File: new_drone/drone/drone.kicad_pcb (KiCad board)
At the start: 2 copper layers, 100 x 100 mm, 61 parts, among them J1 Conn_01x06, J2 XT60-M, SW1 SW_Push_Open, SW2 SW_Push_Open, U1 MPU-6050, U2 ESP32-WROOM-32, U3 MCP8063, U4 BMP280, U5 MCP8063, U6 MCP8063, U7 MCP8063, U9 LM1117MP-3.3

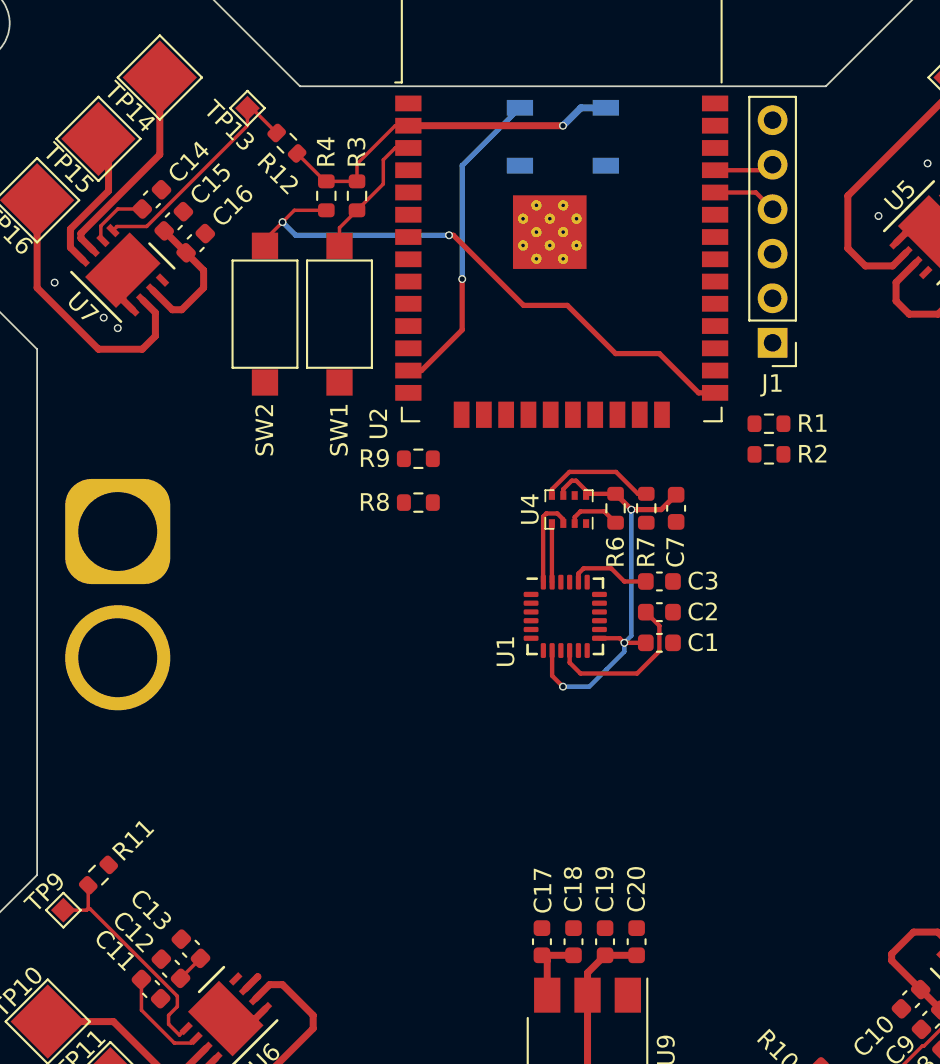
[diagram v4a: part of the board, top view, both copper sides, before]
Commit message: add openmv cam pin
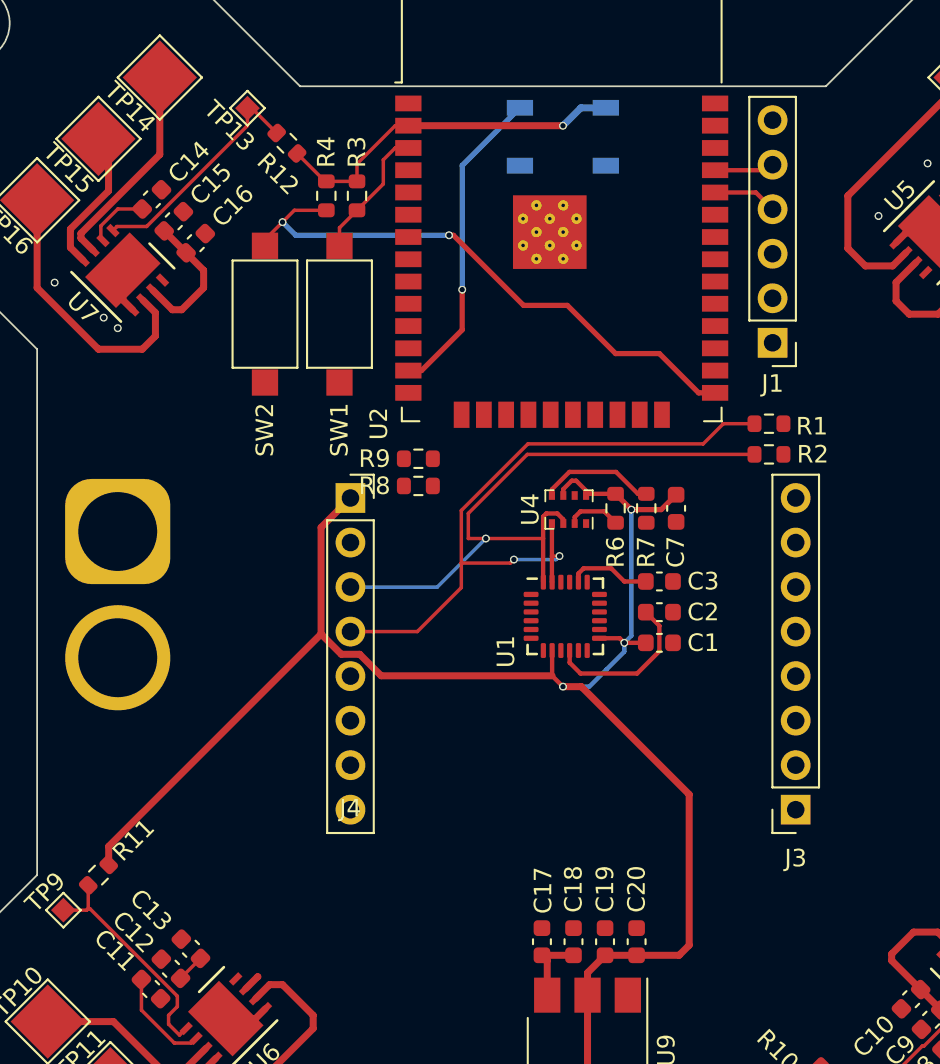
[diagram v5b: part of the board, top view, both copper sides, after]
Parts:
- added J3: Conn_01x08_Pin, Connector_PinSocket_2.54mm:PinSocket_1x08_P2.54mm_Vertical, F.Cu at (163.3, 111.3)
- added J4: Conn_01x08_Pin, Connector_PinSocket_2.54mm:PinSocket_1x08_P2.54mm_Vertical, F.Cu at (137.9, 93.5)
- moved R8 0.95 mm to (141.8, 92.8)
- turned R1 to 180 degrees
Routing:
- net +3.3V: track 71.8 -> 134.1 mm
- net SCL: track 3.35 -> 40.1 mm, vias 0 -> 2
- net SDA: track 5.34 -> 37.6 mm, vias 0 -> 1

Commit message: text on new drone
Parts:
- moved C11 0.14 mm to (126.4, 121.6), turned to 135 degrees
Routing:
- net +BATT: track 32.6 -> 175.0 mm, vias 0 -> 2
- net +3.3V: track 134.1 -> 198.3 mm, vias 4 -> 7
- net MOTOR_2: track 0.00 -> 62.5 mm, vias 0 -> 2
- net MOTOR_3: track 0.00 -> 43.4 mm, vias 0 -> 2
- net MOTOR_1: track 0.00 -> 32.1 mm, vias 0 -> 2
- net SCL: track 40.1 -> 58.6 mm, vias 2 -> 4
- net BAT_LEVEL: track 0.00 -> 18.3 mm
- net SDA: track 37.6 -> 52.4 mm, vias 1 -> 3
- net MOTOR_4: track 0.00 -> 14.6 mm, vias 0 -> 2
- net GND: track 9.99 -> 20.3 mm, vias 5 -> 20
- net Net-(U6-Vbias): track 5.75 -> 0.00 mm
- net Net-(SW2-A): track 33.3 -> 33.9 mm
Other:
- outline, holes or cut-outs redrawn

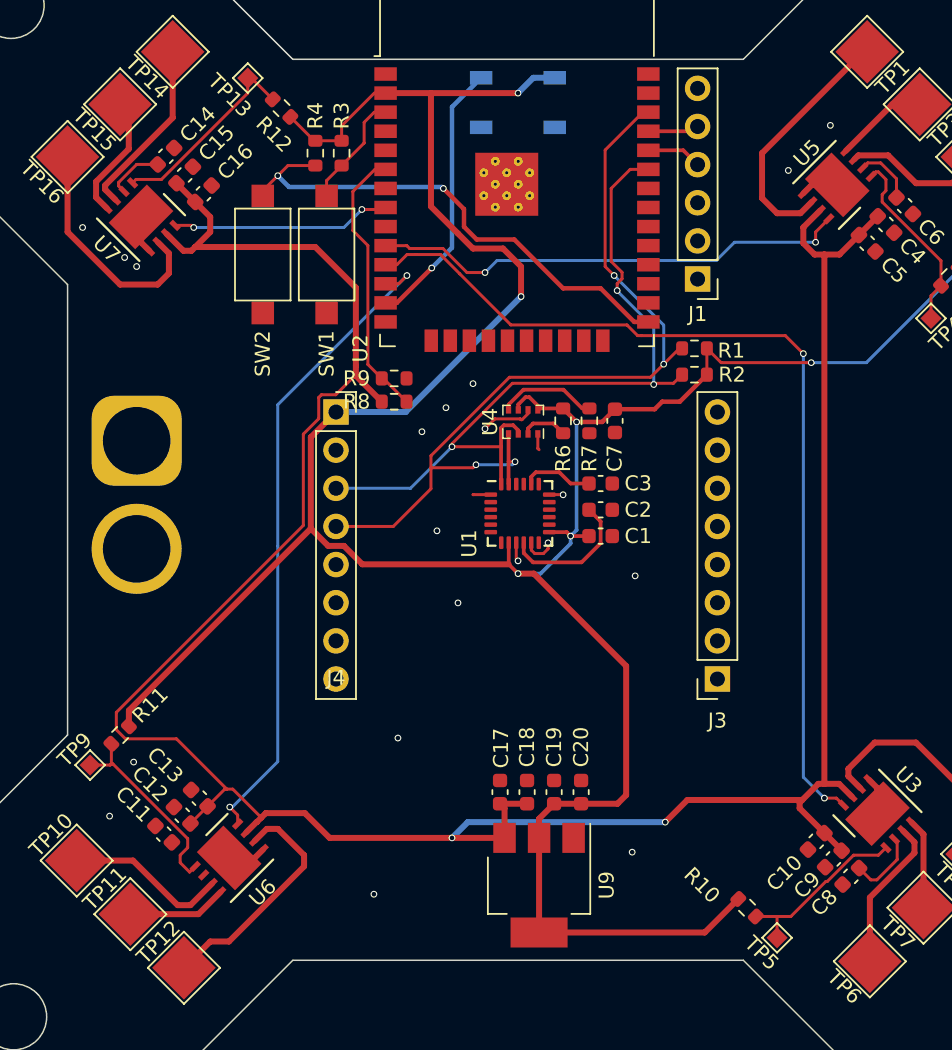
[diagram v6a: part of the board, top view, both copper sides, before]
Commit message: mpu6050 to 9250
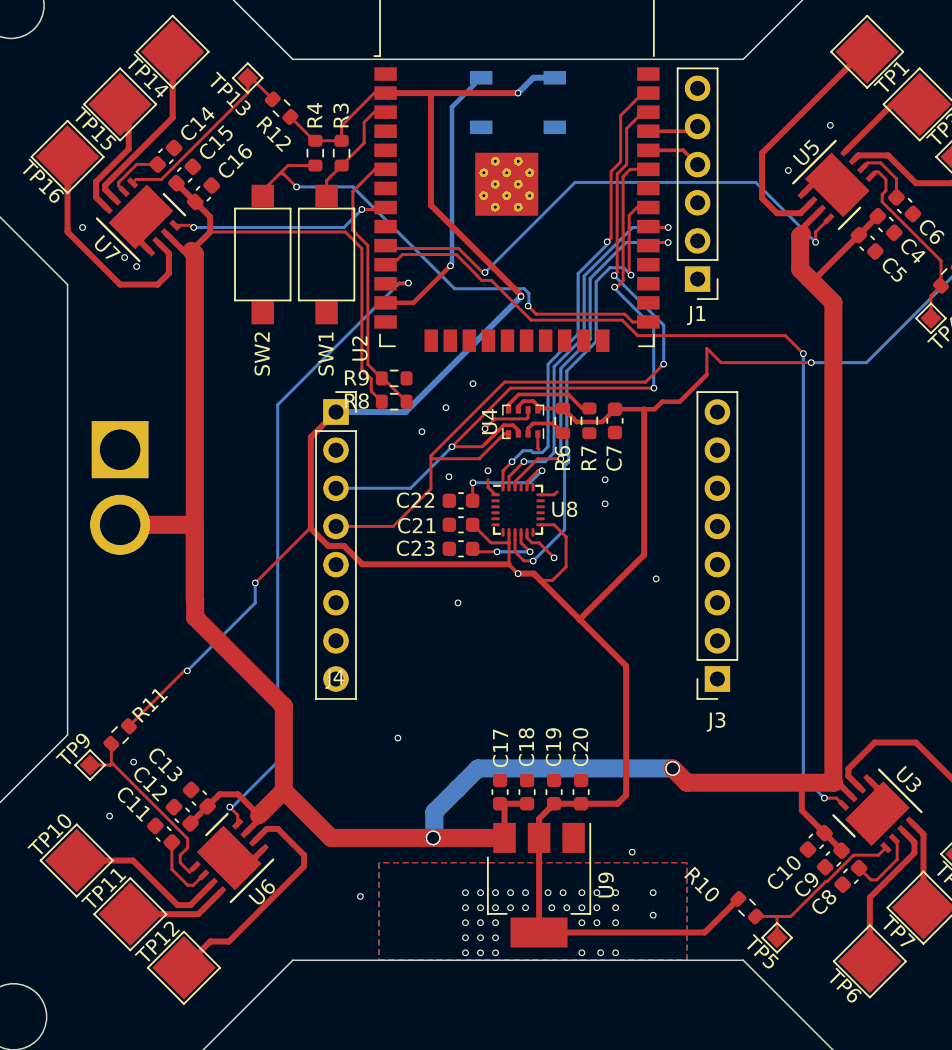
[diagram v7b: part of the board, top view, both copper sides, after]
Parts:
- removed C1, C2, C3: C, Capacitor_SMD:C_0603_1608Metric
- removed R1, R2: R_Small, Resistor_SMD:R_0603_1608Metric
- removed U1: MPU-6050, Sensor_Motion:InvenSense_QFN-24_4x4mm_P0.5mm
- added C21: C, Capacitor_SMD:C_0603_1608Metric, F.Cu at (146.2, 101.0)
- added C22: C, Capacitor_SMD:C_0603_1608Metric, F.Cu at (146.2, 99.4)
- added C23: C, Capacitor_SMD:C_0603_1608Metric, F.Cu at (146.2, 102.6)
- added U8: MPU-9250, Sensor_Motion:InvenSense_QFN-24_3x3mm_P0.4mm, F.Cu at (150.0, 100.0)
- J2: value XT60-M -> XT30PW-M; footprint Connector_AMASS:AMASS_XT60-M_1x02_P7.20mm_Vertical -> Connector_AMASS:AMASS_XT30U-F_1x02_P5.0mm_Vertical
- moved J2 1.25 mm to (123.5, 96.0)
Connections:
- J2 pad 1: (no net) -> GND
- J2 pad 2: (no net) -> +BATT
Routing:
- net MISO: track 0.00 -> 31.6 mm, vias 0 -> 2
- net MOSI: track 0.00 -> 31.4 mm, vias 0 -> 2
- net SCK: track 0.00 -> 25.3 mm, vias 0 -> 2
- net SS: track 0.00 -> 24.5 mm, vias 0 -> 2
- net +BATT: track 175.0 -> 191.3 mm
- net Net-(U1-REGOUT): track 9.14 -> 0.00 mm
- net +3.3V: track 198.3 -> 207.2 mm, vias 7 -> 44
- net Net-(U8-RESV_GND): track 0.00 -> 7.81 mm, vias 0 -> 2
- net SCL: track 58.6 -> 52.7 mm, vias 4 -> 2
- net SDA: track 52.4 -> 46.7 mm
- net Net-(U8-REGOUT): track 0.00 -> 5.46 mm, vias 0 -> 2
- net Net-(U1-CPOUT): track 4.77 -> 0.00 mm
- net Net-(U6-Vbias): track 0.00 -> 4.64 mm
- net MOTOR_1: track 32.1 -> 35.4 mm
- net Net-(D1-DIN): track 18.1 -> 18.7 mm
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- added copper zone on B.Cu, net +3.3V
- added copper zone on F.Cu, net +3.3V

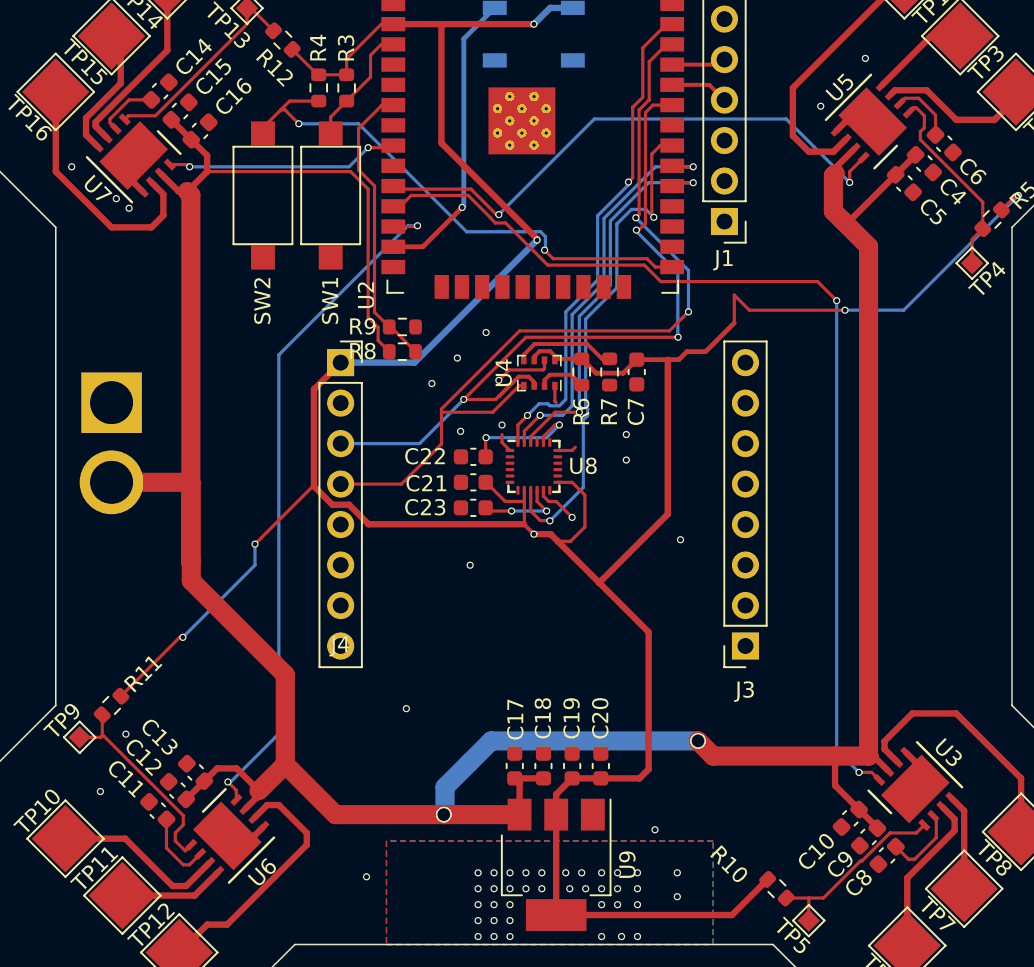
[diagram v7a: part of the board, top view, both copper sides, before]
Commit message: update wiring
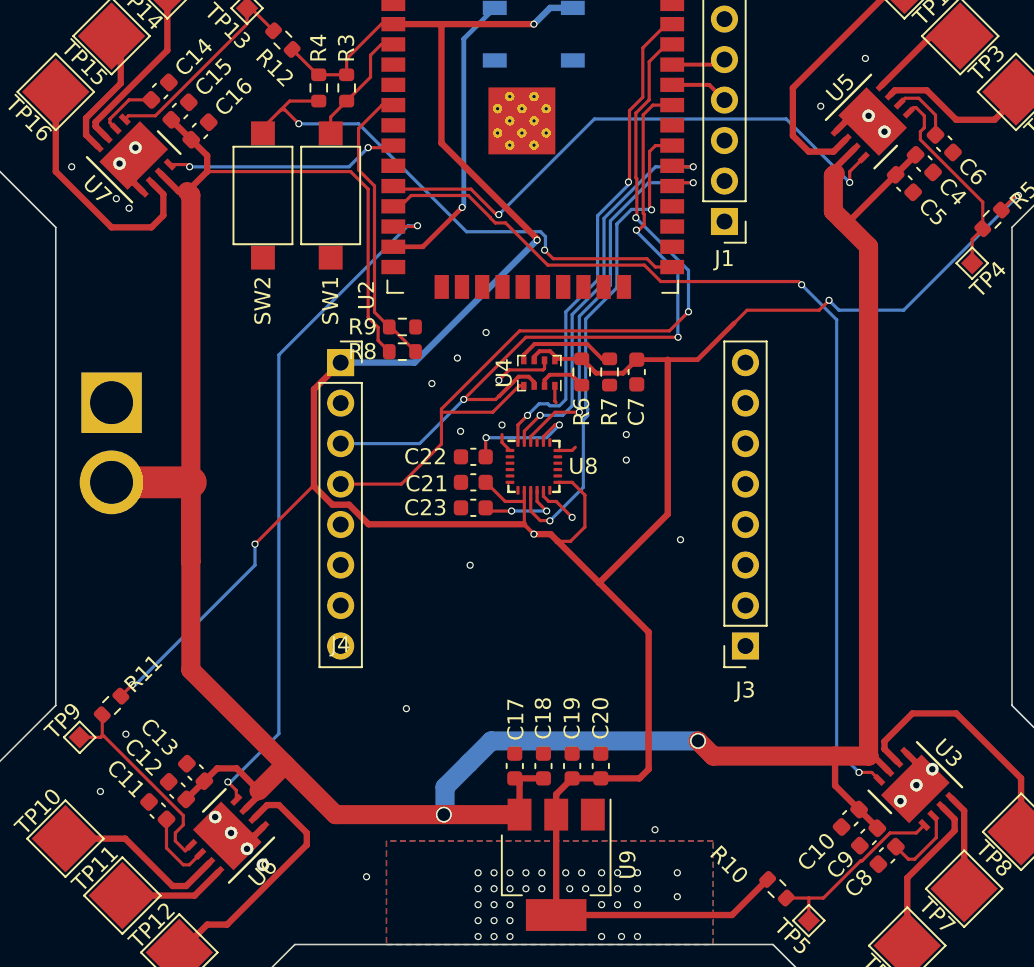
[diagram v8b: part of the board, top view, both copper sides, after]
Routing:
- net GND: track 19.9 -> 21.3 mm, vias 21 -> 32
- net +3.3V: track 207.2 -> 205.9 mm
- net MOTOR_2: track 62.5 -> 61.8 mm
- net MISO: track 31.6 -> 31.1 mm
